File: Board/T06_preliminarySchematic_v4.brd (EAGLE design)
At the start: 59.4 x 80 mm, 57 parts, among them M1 SSW-102-02-S-S, M2 SSW-102-02-S-S, Q3 2n3904, U1 ATMEGA328P_PDIP, X1 SSW-105-02-S-S, X2 SSW-102-02-S-S

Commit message: board minor changes
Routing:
- net GND: track 60.3 -> 55.7 mm
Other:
- board text added: "D"
- board text added: "ECHO"
- board text added: "G"
- board text added: "GND"
- board text added: "S"
- board text added: "TRIG"
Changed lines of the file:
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@@
 <layer number="25" name="tNames" color="7" fill="1" visible="yes" active="yes"/>
 <layer number="26" name="bNames" color="7" fill="1" visible="yes" active="yes"/>
-<layer number="27" name="tValues" color="7" fill="1" visible="yes" active="yes"/>
+<layer number="27" name="tValues" color="7" fill="1" visible="no" active="yes"/>
 <layer number="28" name="bValues" color="7" fill="1" visible="yes" active="yes"/>
 <layer number="29" name="tStop" color="7" fill="3" visible="no" active="yes"/>
@@
 <text x="32.385" y="19.685" size="1.016" layer="25">3v3</text>
 <text x="32.385" y="6.985" size="1.016" layer="25">5v</text>
-<hole x="55.88" y="3.175" drill="0.7"/>
+<hole x="55.88" y="2.54" drill="0.7"/>
 <hole x="8.89" y="2.54" drill="0.7"/>
-<hole x="6.985" y="76.2" drill="0.7"/>
+<hole x="3.81" y="77.47" drill="0.7"/>
 <hole x="55.88" y="77.47" drill="0.7"/>
 <hole x="33.655" y="45.72" drill="0.7"/>
+<text x="4.445" y="2.54" size="0.6096" layer="25" rot="R270">GND</text>
+<text x="42.545" y="6.985" size="0.6096" layer="25" rot="R270">GND</text>
+<text x="52.705" y="67.945" size="0.6096" layer="25">GND</text>
+<text x="50.165" y="55.245" size="0.6096" layer="25">GND</text>
+<text x="47.625" y="42.545" size="0.6096" layer="25">GND</text>
+<text x="48.895" y="77.47" size="0.6096" layer="25">GND</text>
+<text x="43.815" y="77.47" size="0.6096" layer="25">GND</text>
+<text x="52.705" y="65.405" size="0.6096" layer="25">ECHO</text>
+<text x="50.165" y="52.705" size="0.6096" layer="25">ECHO</text>
+<text x="47.625" y="40.005" size="0.6096" layer="25">ECHO</text>
+<text x="52.705" y="62.865" size="0.6096" layer="25">TRIG</text>
+<text x="47.625" y="37.465" size="0.6096" layer="25">TRIG</text>
+<text x="50.165" y="49.53" size="0.6096" layer="25">TRIG</text>
+<text x="30.48" y="78.105" size="0.6096" layer="25">G</text>
+<text x="27.305" y="73.025" size="0.6096" layer="25">D</text>
+<text x="33.02" y="73.025" size="0.6096" layer="25">S</text>
 </plain>
 <attributes>
@@
 <attribute name="MF" value="" x="2.54" y="3.175" size="1.778" layer="27" rot="R270" display="off"/>
 <attribute name="OC_NEWARK" value="11P9351" x="2.54" y="3.175" size="1.778" layer="27" rot="R270" display="off"/>
-<attribute name="NAME" x="5.715" y="0" size="1.27" layer="25" rot="R90"/>
+<attribute name="NAME" x="5.715" y="0.635" size="1.27" layer="25"/>
+<attribute name="VALUE" x="1.27" y="-1.27" size="1.27" layer="27"/>
 </element>
 <element name="Q3" library="SparkFun-DiscreteSemi" package="TO-92" value="2n3904" x="30.48" y="74.93" smashed="yes">
@@
 <element name="TP22" library="testpad" package="P1-13" value="TPPAD1-13" x="22.86" y="41.91" smashed="yes" rot="R180">
 <attribute name="TP_SIGNAL_NAME" value="" x="24.13" y="44.45" size="1" layer="37" rot="R180"/>
-<attribute name="NAME" x="23.876" y="40.64" size="1.27" layer="25" ratio="10" rot="R180"/>
+<attribute name="NAME" x="25.146" y="45.085" size="1.27" layer="25" ratio="10" rot="R180"/>
 <attribute name="VALUE" x="22.86" y="41.91" size="0.0254" layer="27" rot="R180"/>
 </element>
@@
 <wire x1="6.4008" y1="48.7426" x2="6.35" y2="48.275" width="0.3048" layer="1"/>
 <wire x1="16.4846" y1="72.0852" x2="16.51" y2="71.975" width="0.3048" layer="1"/>
-<wire x1="27.6606" y1="41.91" x2="27.559" y2="41.3766" width="0.3048" layer="1"/>
-<wire x1="22.86" y1="41.91" x2="27.6606" y2="41.91" width="0.3048" layer="1"/>
+<wire x1="22.5806" y1="41.91" x2="23.114" y2="42.0116" width="0.3048" layer="1"/>
+<wire x1="22.86" y1="41.91" x2="22.5806" y2="41.91" width="0.3048" layer="1"/>
 <wire x1="30.734" y1="22.0726" x2="30.734" y2="17.3228" width="0.3048" layer="1"/>
 <wire x1="30.4546" y1="16.637" x2="30.734" y2="22.0726" width="0.3048" layer="1"/>
@@
 <wire x1="9.779" y1="42.7482" x2="9.525" y2="42.545" width="0.3048" layer="16"/>
 <polygon width="0.4064" layer="16" isolate="0.254">
-<vertex x="-1.27" y="80.645"/>
-<vertex x="61.595" y="80.645"/>
-<vertex x="61.595" y="-1.27"/>
-<vertex x="-1.27" y="-1.27"/>
-<vertex x="-1.27" y="1.905"/>
+<vertex x="0.635" y="79.375"/>
+<vertex x="59.055" y="79.375"/>
+<vertex x="59.055" y="0.635"/>
+<vertex x="0.635" y="0.635"/>
 </polygon>
 <via x="8.255" y="12.7" extent="1-16" drill="0.6" shape="square"/>
@@
 <via x="20.955" y="5.08" extent="1-16" drill="0.6"/>
 <polygon width="0.6096" layer="1" isolate="0.254">
-<vertex x="-1.905" y="81.28"/>
-<vertex x="62.23" y="81.28"/>
-<vertex x="62.23" y="-1.27"/>
-<vertex x="-1.905" y="-1.27"/>
-<vertex x="-1.905" y="-0.635"/>
-<vertex x="-1.905" y="80.645"/>
+<vertex x="0.635" y="79.375"/>
+<vertex x="59.055" y="79.375"/>
+<vertex x="59.055" y="0.635"/>
+<vertex x="0.635" y="0.635"/>
 </polygon>
 <via x="53.34" y="38.735" extent="1-16" drill="0.6"/>
@@
 <wire x1="35.5346" y1="17.415" x2="37.735" y2="17.145" width="1.016" layer="1"/>
 <wire x1="8.255" y1="5.5" x2="9.945" y2="5.5" width="0.6096" layer="1"/>
-<wire x1="9.945" y1="5.5" x2="18.415" y2="13.97" width="0.6096" layer="1"/>
-<wire x1="26.305" y1="17.145" x2="18.415" y2="13.97" width="0.6096" layer="1"/>
+<wire x1="9.945" y1="5.5" x2="18.415" y2="13.335" width="1.016" layer="1"/>
+<wire x1="26.305" y1="17.145" x2="18.415" y2="13.335" width="1.016" layer="1"/>
 <wire x1="2.54" y1="4.445" x2="2.54" y2="7.62" width="0.6096" layer="1"/>
-<wire x1="2.54" y1="7.62" x2="8.255" y2="5.5" width="0.6096" layer="1"/>
+<wire x1="2.54" y1="7.62" x2="8.255" y2="5.5" width="1.016" layer="1"/>
 </signal>
 <signal name="+3V3">

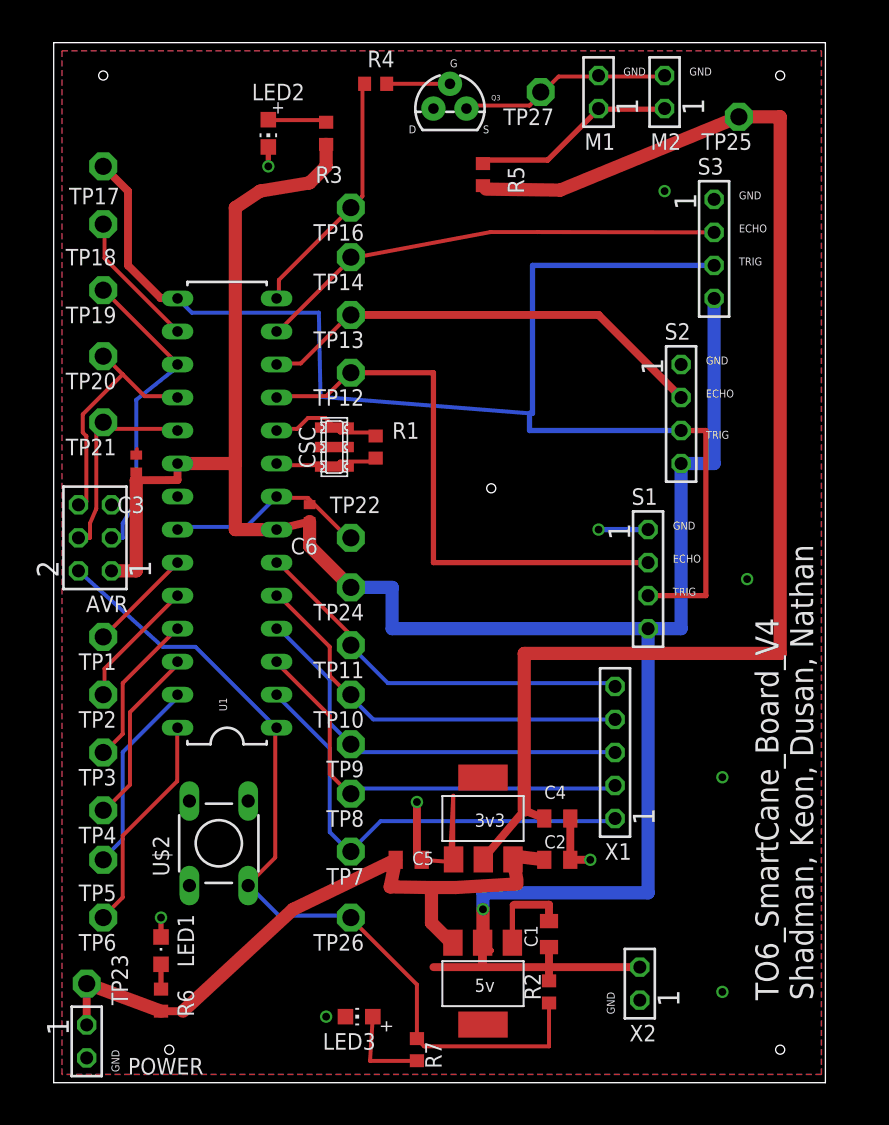
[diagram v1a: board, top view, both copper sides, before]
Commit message: Built the prototype. The sensor doesnt allow us the trigger all the sensors in parallel. So we are using individual pins to trigger the sensors. That is reflected in this revision
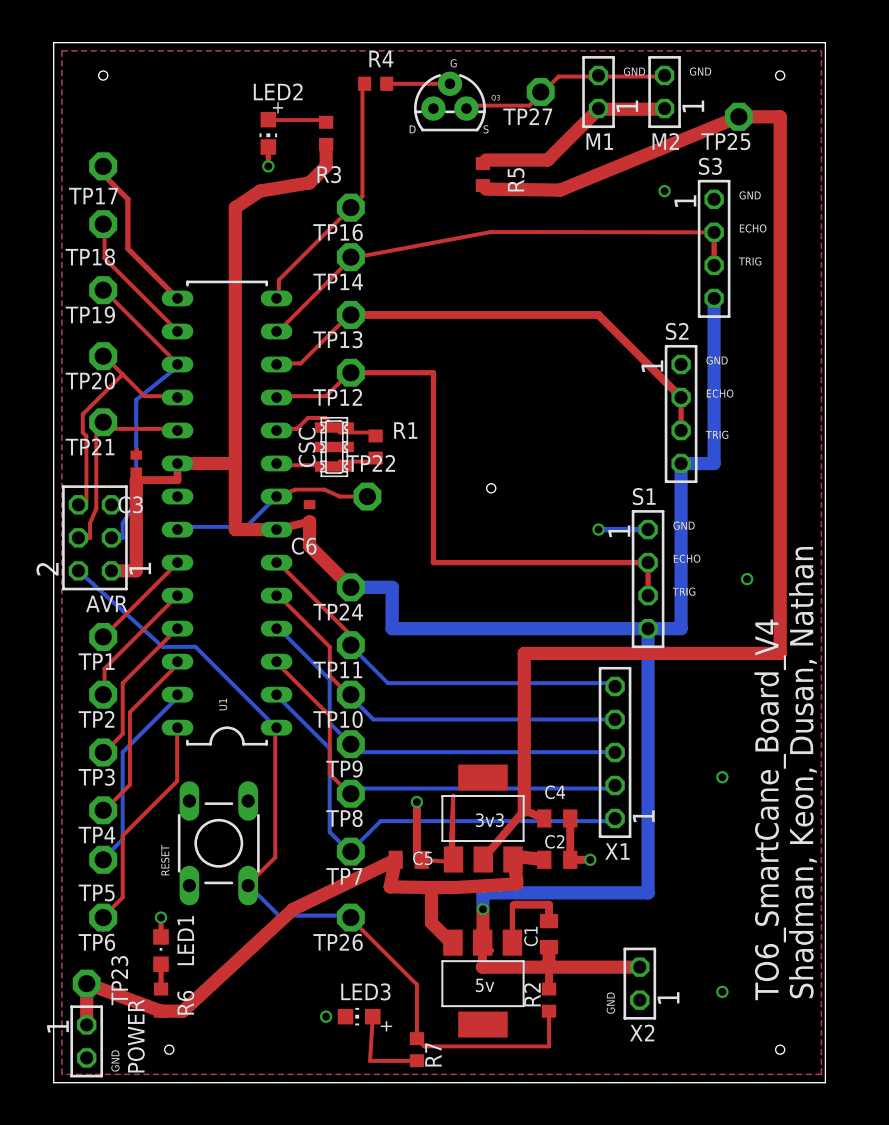
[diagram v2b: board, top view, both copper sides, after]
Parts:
- moved TP22 3.42 mm to (24.1, 45.1)
- moved R2 0.64 mm to (38.1, 6.35)
- renumbered U$2 to RESET
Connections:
- removed net TRIG: S1.3, S2.3, S3.3, TP17.TP, U1.15
- new net N$15: TP17.TP, U1.15
- net ECHO1: now also S1.3
- net ECHO2: now also S2.3
- net ECHO3: now also S3.3
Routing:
- net TRIG: track 104.9 -> 0.00 mm
- net N$15: track 0.00 -> 12.5 mm
- net +5V: track 185.6 -> 182.4 mm
- net ECHO3: track 36.3 -> 38.8 mm
- net ECHO2: track 35.3 -> 37.8 mm
- net ECHO1: track 43.9 -> 46.5 mm
- net RESET: track 67.1 -> 66.5 mm

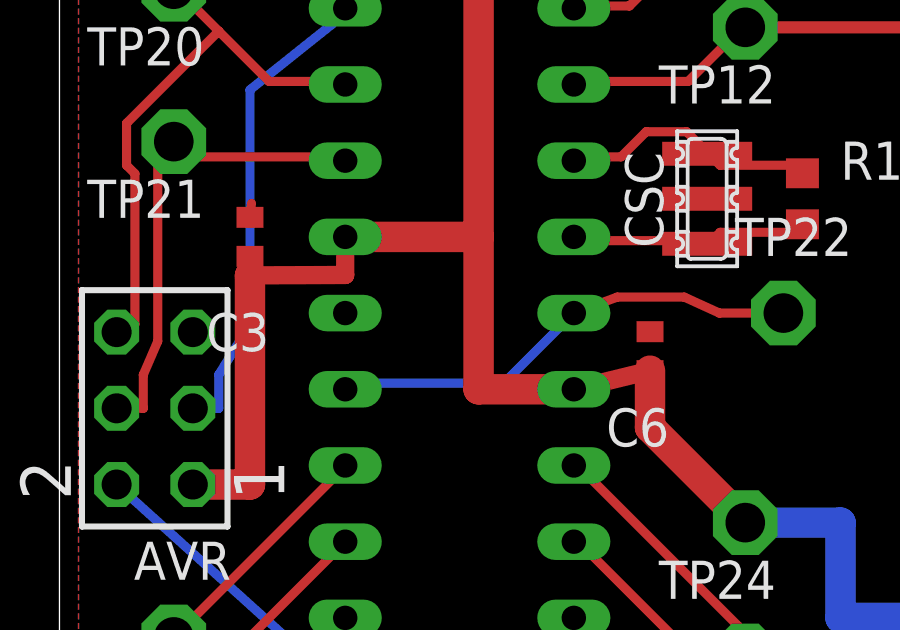
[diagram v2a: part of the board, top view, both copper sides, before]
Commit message: Made changes to the cap size from 1005 to 0805
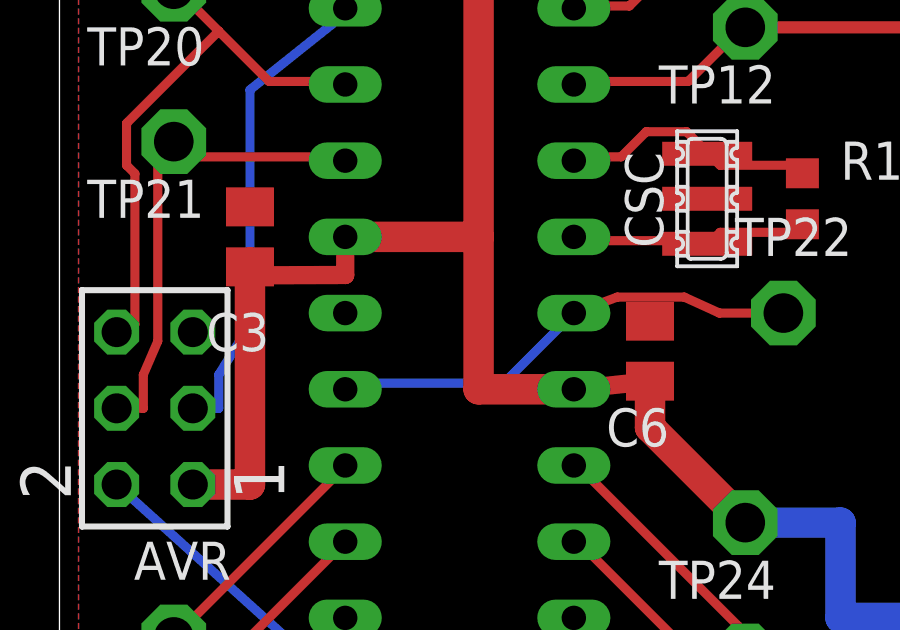
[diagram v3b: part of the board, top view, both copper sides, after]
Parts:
- C3, C6: device eagle-ltspice:C1005 -> rcl:C0805K
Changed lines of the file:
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@@
 <attribute name="VALUE" x="37.735" y="15.245" size="1.016" layer="27"/>
 </element>
-<element name="C3" library="eagle-ltspice" package="C1005" value="100n" x="6.35" y="47.625" smashed="yes" rot="R90">
-<attribute name="SPICEPREFIX" value="C" x="6.35" y="47.625" size="1.778" layer="27" rot="R90" display="off"/>
-<attribute name="SPICEMODEL" value="NONE" x="6.35" y="47.625" size="1.778" layer="27" rot="R90" display="off"/>
+<element name="C3" library="rcl" package="C0805K" value="100n" x="6.35" y="47.625" smashed="yes" rot="R90">
 <attribute name="NAME" x="6.985" y="45.085" size="1.27" layer="25" font="vector" rot="R180"/>
 <attribute name="VALUE" x="8.255" y="46.99" size="1.27" layer="27" rot="R90"/>
@@
 <attribute name="VALUE" x="26.305" y="15.245" size="1.016" layer="27"/>
 </element>
-<element name="C6" library="eagle-ltspice" package="C1005" value="100n" x="19.685" y="43.815" smashed="yes" rot="R90">
-<attribute name="SPICEPREFIX" value="C" x="19.685" y="43.815" size="1.778" layer="27" rot="R90" display="off"/>
-<attribute name="SPICEMODEL" value="NONE" x="19.685" y="43.815" size="1.778" layer="27" rot="R90" display="off"/>
+<element name="C6" library="rcl" package="C0805K" value="100n" x="19.685" y="43.815" smashed="yes" rot="R90">
 <attribute name="NAME" x="20.32" y="41.91" size="1.27" layer="25" rot="R180"/>
 <attribute name="VALUE" x="24.13" y="44.45" size="1.27" layer="27" rot="R180"/>
@@
 <wire x1="10.6172" y1="15.0876" x2="10.4394" y2="15.1638" width="0.3048" layer="16"/>
 <wire x1="21.59" y1="48.895" x2="20.3454" y2="48.895" width="0.3048" layer="1"/>
-<wire x1="6.4008" y1="48.7426" x2="6.35" y2="48.275" width="0.3048" layer="1"/>
+<wire x1="6.4008" y1="48.7426" x2="6.35" y2="48.625" width="0.3048" layer="1"/>
 <wire x1="16.4846" y1="72.0852" x2="16.51" y2="71.975" width="0.3048" layer="1"/>
 <wire x1="23.8506" y1="45.085" x2="24.384" y2="45.1866" width="0.3048" layer="1"/>
@@
 <wire x1="45.085" y1="8.89" x2="38.1" y2="8.89" width="1.016" layer="1"/>
 <wire x1="9.525" y1="46.355" x2="6.3627" y2="46.3423" width="0.6096" layer="1"/>
-<wire x1="6.35" y1="46.975" x2="6.35" y2="46.99" width="0.6096" layer="1"/>
+<wire x1="6.35" y1="46.625" x2="6.35" y2="46.99" width="0.6096" layer="1"/>
 <wire x1="6.35" y1="46.99" x2="6.3627" y2="46.3423" width="0.4064" layer="1"/>
 <wire x1="9.525" y1="46.355" x2="9.525" y2="47.625" width="0.6096" layer="1"/>
-<wire x1="19.685" y1="43.165" x2="17.145" y2="42.545" width="0.6096" layer="1"/>
+<wire x1="19.685" y1="42.815" x2="17.145" y2="42.545" width="0.6096" layer="1"/>
 <wire x1="32.9946" y1="10.7696" x2="33.6042" y2="10.16" width="0.4064" layer="1"/>
 <wire x1="33.6042" y1="10.16" x2="33.655" y2="10.16" width="0.4064" layer="1"/>
@@
 <wire x1="26.035" y1="38.1" x2="22.86" y2="38.1" width="1.016" layer="16"/>
 <wire x1="22.86" y1="38.1" x2="19.685" y2="41.275" width="1.016" layer="1"/>
-<wire x1="19.685" y1="41.275" x2="19.685" y2="43.165" width="1.016" layer="1"/>
+<wire x1="19.685" y1="41.275" x2="19.685" y2="42.815" width="1.016" layer="1"/>
 <wire x1="17.145" y1="42.545" x2="13.97" y2="42.545" width="1.016" layer="1"/>
 <wire x1="13.97" y1="42.545" x2="13.97" y2="47.625" width="1.016" layer="1"/>
